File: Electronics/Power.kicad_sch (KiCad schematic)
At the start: 17 parts, among them U1 R-78C15-1.0, U401 R-78C5.0-1.0

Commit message: Updated Design
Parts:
- added H408, H409, H410, H411: MountingHole, MountingHole:MountingHole_3.2mm_M3_DIN965, symbol Mechanical:MountingHole
- C401, C403, C405: value C -> 4u7; footprint Capacitor_SMD:C_0603_1608Metric_Pad1.08x0.95mm_HandSolder -> Resistor_SMD:R_0805_2012Metric_Pad1.20x1.40mm_HandSolder
- C402, C404, C406, C407: value C -> 100n
- C408: value C -> 10u; footprint Capacitor_SMD:C_0603_1608Metric_Pad1.08x0.95mm_HandSolder -> Resistor_SMD:R_0805_2012Metric_Pad1.20x1.40mm_HandSolder
- renumbered U1 to U402
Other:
- moved on the sheet: C408
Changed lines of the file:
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@@
   (junction (at 199.39 53.34) (diameter 0) (color 0 0 0 0)
   )
-  (junction (at 250.19 53.34) (diameter 0) (color 0 0 0 0)
+  (junction (at 252.095 53.34) (diameter 0) (color 0 0 0 0)
   )
   (wire (pts (xy 209.55 53.34) (xy 209.55 55.88))
@@
     (stroke (width 0) (type default) (color 0 0 0 0))
   )
-  (wire (pts (xy 250.19 67.31) (xy 241.3 67.31))
+  (wire (pts (xy 252.095 67.31) (xy 241.3 67.31))
     (stroke (width 0) (type default) (color 0 0 0 0))
   )
@@
     (stroke (width 0) (type default) (color 0 0 0 0))
   )
-  (wire (pts (xy 250.19 53.34) (xy 259.08 53.34))
+  (wire (pts (xy 252.095 53.34) (xy 259.08 53.34))
     (stroke (width 0) (type default) (color 0 0 0 0))
   )
@@
     (stroke (width 0) (type default) (color 0 0 0 0))
   )
-  (wire (pts (xy 250.19 63.5) (xy 250.19 67.31))
-    (stroke (width 0) (type default) (color 0 0 0 0))
-  )
-  (wire (pts (xy 250.19 53.34) (xy 250.19 55.88))
+  (wire (pts (xy 252.095 63.5) (xy 252.095 67.31))
+    (stroke (width 0) (type default) (color 0 0 0 0))
+  )
+  (wire (pts (xy 252.095 53.34) (xy 252.095 55.88))
     (stroke (width 0) (type default) (color 0 0 0 0))
   )
@@
     (stroke (width 0) (type default) (color 0 0 0 0))
   )
-  (wire (pts (xy 241.3 53.34) (xy 250.19 53.34))
+  (wire (pts (xy 241.3 53.34) (xy 252.095 53.34))
     (stroke (width 0) (type default) (color 0 0 0 0))
   )
@@
     (pin "3")
   )
+  (symbol (lib_name "MountingHole_1") (lib_id "Mechanical:MountingHole") (at 135.89 191.77 0) (unit 1)
+    (in_bom yes) (on_board yes) (fields_autoplaced)
+    (property "Reference" "H409" (id 0) (at 138.43 190.8615 0)
+      (effects (font (size 1.27 1.27)) (justify left))
+    )
+    (property "Value" "MountingHole" (id 1) (at 138.43 193.6366 0)
+      (effects (font (size 1.27 1.27)) (justify left) hide)
+    )
+    (property "Footprint" "MountingHole:MountingHole_3.2mm_M3_DIN965" (id 2) (at 135.89 191.77 0)
+      (effects (font (size 1.27 1.27)) hide)
+    )
+    (property "Datasheet" "~" (id 3) (at 135.89 191.77 0)
+      (effects (font (size 1.27 1.27)) hide)
+    )
+  )
   (symbol (lib_name "MountingHole_1") (lib_id "Mechanical:MountingHole") (at 162.56 161.29 0) (unit 1)
     (in_bom yes) (on_board yes) (fields_autoplaced)
@@
       (effects (font (size 1.27 1.27)) (justify left))
     )
-    (property "Value" "C" (id 1) (at 202.311 61.5566 0)
-      (effects (font (size 1.27 1.27)) (justify left))
-    )
-    (property "Footprint" "Capacitor_SMD:C_0603_1608Metric_Pad1.08x0.95mm_HandSolder" (id 2) (at 200.3552 63.5 0)
+    (property "Value" "4u7" (id 1) (at 202.311 61.5566 0)
+      (effects (font (size 1.27 1.27)) (justify left))
+    )
+    (property "Footprint" "Resistor_SMD:R_0805_2012Metric_Pad1.20x1.40mm_HandSolder" (id 2) (at 200.3552 63.5 0)
       (effects (font (size 1.27 1.27)) hide)
     )
@@
       (effects (font (size 1.27 1.27)) (justify left))
     )
-    (property "Value" "C" (id 1) (at 96.901 61.5566 0)
-      (effects (font (size 1.27 1.27)) (justify left))
-    )
-    (property "Footprint" "Capacitor_SMD:C_0603_1608Metric_Pad1.08x0.95mm_HandSolder" (id 2) (at 94.9452 63.5 0)
+    (property "Value" "4u7" (id 1) (at 96.901 61.5566 0)
+      (effects (font (size 1.27 1.27)) (justify left))
+    )
+    (property "Footprint" "Resistor_SMD:R_0805_2012Metric_Pad1.20x1.40mm_HandSolder" (id 2) (at 94.9452 63.5 0)
       (effects (font (size 1.27 1.27)) hide)
     )
@@
   (symbol (lib_id "Regulator_Switching:R-78C15-1.0") (at 125.73 53.34 0) (unit 1)
     (in_bom yes) (on_board yes) (fields_autoplaced)
-    (property "Reference" "U1" (id 0) (at 125.73 45.72 0))
-    (property "Value" "R-78C15-1.0" (id 1) (at 125.73 48.26 0))
+    (property "Reference" "U402" (id 0) (at 125.73 47.4685 0))
+    (property "Value" "R-78C15-1.0" (id 1) (at 125.73 50.2436 0))
     (property "Footprint" "Converter_DCDC:Converter_DCDC_RECOM_R-78E-0.5_THT" (id 2) (at 127 59.69 0)
       (effects (font (size 1.27 1.27) italic) (justify left) hide)
@@
     (pin "3")
   )
+  (symbol (lib_name "MountingHole_1") (lib_id "Mechanical:MountingHole") (at 146.685 184.785 0) (unit 1)
+    (in_bom yes) (on_board yes) (fields_autoplaced)
+    (property "Reference" "H410" (id 0) (at 149.225 183.8765 0)
+      (effects (font (size 1.27 1.27)) (justify left))
+    )
+    (property "Value" "MountingHole" (id 1) (at 149.225 186.6516 0)
+      (effects (font (size 1.27 1.27)) (justify left) hide)
+    )
+    (property "Footprint" "MountingHole:MountingHole_3.2mm_M3_DIN965" (id 2) (at 146.685 184.785 0)
+      (effects (font (size 1.27 1.27)) hide)
+    )
+    (property "Datasheet" "~" (id 3) (at 146.685 184.785 0)
+      (effects (font (size 1.27 1.27)) hide)
+    )
+  )
   (symbol (lib_id "Device:C") (at 104.14 59.69 0) (unit 1)
     (in_bom yes) (on_board yes) (fields_autoplaced)
@@
       (effects (font (size 1.27 1.27)) (justify left))
     )
-    (property "Value" "C" (id 1) (at 107.061 61.5566 0)
+    (property "Value" "100n" (id 1) (at 107.061 61.5566 0)
       (effects (font (size 1.27 1.27)) (justify left))
     )
@@
       (effects (font (size 1.27 1.27)) (justify left))
     )
-    (property "Value" "C" (id 1) (at 244.221 61.5566 0)
+    (property "Value" "100n" (id 1) (at 244.221 61.5566 0)
       (effects (font (size 1.27 1.27)) (justify left))
     )
@@
       (effects (font (size 1.27 1.27)) (justify left))
     )
-    (property "Value" "C" (id 1) (at 212.471 61.5566 0)
+    (property "Value" "100n" (id 1) (at 212.471 61.5566 0)
       (effects (font (size 1.27 1.27)) (justify left))
     )
@@
       (effects (font (size 1.27 1.27)) (justify left))
     )
-    (property "Value" "C" (id 1) (at 147.701 61.5566 0)
-      (effects (font (size 1.27 1.27)) (justify left))
-    )
-    (property "Footprint" "Capacitor_SMD:C_0603_1608Metric_Pad1.08x0.95mm_HandSolder" (id 2) (at 145.7452 63.5 0)
+    (property "Value" "4u7" (id 1) (at 147.701 61.5566 0)
+      (effects (font (size 1.27 1.27)) (justify left))
+    )
+    (property "Footprint" "Resistor_SMD:R_0805_2012Metric_Pad1.20x1.40mm_HandSolder" (id 2) (at 145.7452 63.5 0)
       (effects (font (size 1.27 1.27)) hide)
     )
@@
     (pin "1")
   )
+  (symbol (lib_name "MountingHole_1") (lib_id "Mechanical:MountingHole") (at 135.89 184.785 0) (unit 1)
+    (in_bom yes) (on_board yes) (fields_autoplaced)
+    (property "Reference" "H408" (id 0) (at 138.43 183.8765 0)
+      (effects (font (size 1.27 1.27)) (justify left))
+    )
+    (property "Value" "MountingHole" (id 1) (at 138.43 186.6516 0)
+      (effects (font (size 1.27 1.27)) (justify left) hide)
+    )
+    (property "Footprint" "MountingHole:MountingHole_3.2mm_M3_DIN965" (id 2) (at 135.89 184.785 0)
+      (effects (font (size 1.27 1.27)) hide)
+    )
+    (property "Datasheet" "~" (id 3) (at 135.89 184.785 0)
+      (effects (font (size 1.27 1.27)) hide)
+    )
+  )
   (symbol (lib_id "Device:C") (at 154.94 59.69 0) (unit 1)
     (in_bom yes) (on_board yes) (fields_autoplaced)
@@
       (effects (font (size 1.27 1.27)) (justify left))
     )
-    (property "Value" "C" (id 1) (at 157.861 61.5566 0)
+    (property "Value" "100n" (id 1) (at 157.861 61.5566 0)
       (effects (font (size 1.27 1.27)) (justify left))
     )
@@
     (pin "1")
     (pin "2")
+  )
+  (symbol (lib_name "MountingHole_1") (lib_id "Mechanical:MountingHole") (at 146.685 191.77 0) (unit 1)
+    (in_bom yes) (on_board yes) (fields_autoplaced)
+    (property "Reference" "H411" (id 0) (at 149.225 190.8615 0)
+      (effects (font (size 1.27 1.27)) (justify left))
+    )
+    (property "Value" "MountingHole" (id 1) (at 149.225 193.6366 0)
+      (effects (font (size 1.27 1.27)) (justify left) hide)
+    )
+    (property "Footprint" "MountingHole:MountingHole_3.2mm_M3_DIN965" (id 2) (at 146.685 191.77 0)
+      (effects (font (size 1.27 1.27)) hide)
+    )
+    (property "Datasheet" "~" (id 3) (at 146.685 191.77 0)
+      (effects (font (size 1.27 1.27)) hide)
+    )
   )
   (symbol (lib_id "power:VD") (at 73.66 46.99 0) (unit 1)
@@
     (pin "1")
   )
-  (symbol (lib_id "Device:C") (at 250.19 59.69 0) (unit 1)
-    (in_bom yes) (on_board yes) (fields_autoplaced)
-    (property "Reference" "C408" (id 0) (at 253.111 58.7815 0)
-      (effects (font (size 1.27 1.27)) (justify left))
-    )
-    (property "Value" "C" (id 1) (at 253.111 61.5566 0)
-      (effects (font (size 1.27 1.27)) (justify left))
-    )
-    (property "Footprint" "Capacitor_SMD:C_0603_1608Metric_Pad1.08x0.95mm_HandSolder" (id 2) (at 251.1552 63.5 0)
-      (effects (font (size 1.27 1.27)) hide)
-    )
-    (property "Datasheet" "~" (id 3) (at 250.19 59.69 0)
-      (effects (font (size 1.27 1.27)) hide)
-    )
+  (symbol (lib_id "Device:C") (at 252.095 59.69 0) (unit 1)
+    (in_bom yes) (on_board yes) (fields_autoplaced)
+    (property "Reference" "C408" (id 0) (at 255.016 58.7815 0)
+      (effects (font (size 1.27 1.27)) (justify left))
+    )
+    (property "Value" "10u" (id 1) (at 255.016 61.5566 0)
+      (effects (font (size 1.27 1.27)) (justify left))
+    )
+    (property "Footprint" "Resistor_SMD:R_0805_2012Metric_Pad1.20x1.40mm_HandSolder" (id 2) (at 253.0602 63.5 0)
+      (effects (font (size 1.27 1.27)) hide)
+    )
+    (property "Datasheet" "~" (id 3) (at 252.095 59.69 0)
+      (effects (font (size 1.27 1.27)) hide)
+    )

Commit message: Layout improvements
Signed-off-by: Aki Kuusela <git@findersee.fi>
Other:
- company: (none) -> findersee.fi
- title: (none) -> Motor Controller
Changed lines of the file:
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@@
 (kicad_sch (version 20211123) (generator eeschema)
   (paper "A4")
+  (title_block
+    (title "Motor Controller")
+    (date "2022-02-18")
+    (rev "1.0")
+    (company "findersee.fi")
+  )
   (junction (at 166.37 53.34) (diameter 0) (color 0 0 0 0)
   )

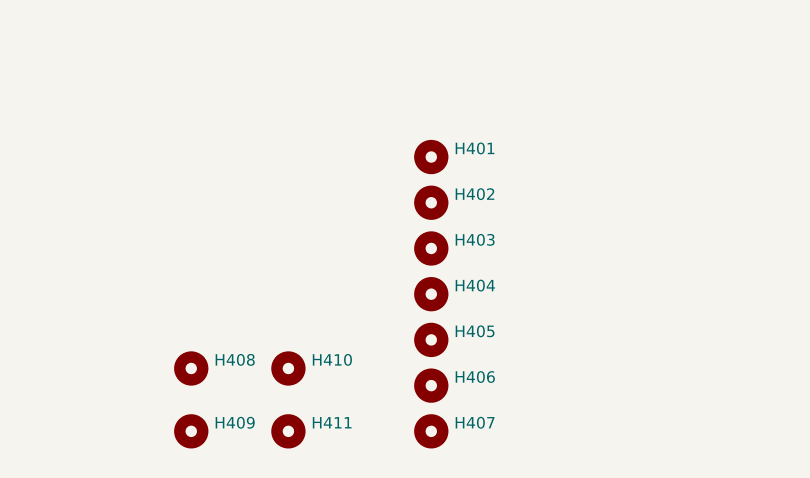
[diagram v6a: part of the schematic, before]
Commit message: Changed capacitor to multi footprint version. Added parallel diodes to MOSFET gate resistors to improve Turn-OFF time.
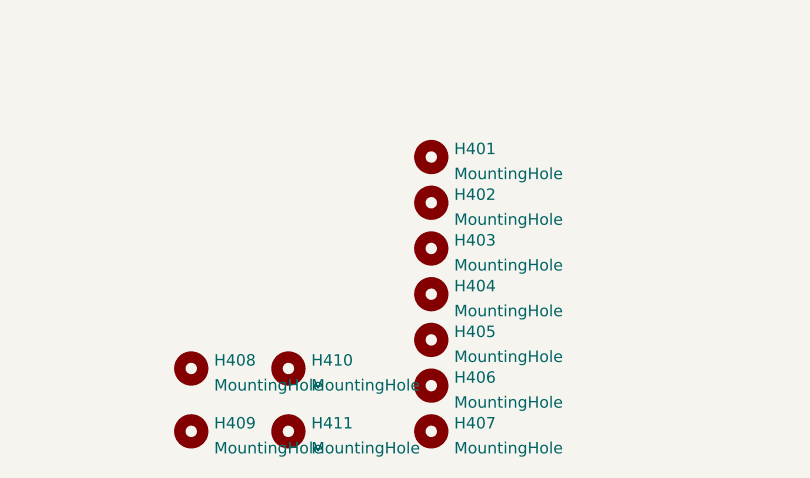
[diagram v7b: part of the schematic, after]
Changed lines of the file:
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@@
     )
     (property "Value" "MountingHole" (id 1) (at 138.43 193.6366 0)
-      (effects (font (size 1.27 1.27)) (justify left) hide)
+      (effects (font (size 1.27 1.27)) (justify left))
     )
     (property "Footprint" "MountingHole:MountingHole_3.2mm_M3_DIN965" (id 2) (at 135.89 191.77 0)
@@
     )
     (property "Value" "MountingHole" (id 1) (at 165.1 163.1566 0)
-      (effects (font (size 1.27 1.27)) (justify left) hide)
+      (effects (font (size 1.27 1.27)) (justify left))
     )
     (property "Footprint" "MountingHole:MountingHole_3.2mm_M3_DIN965" (id 2) (at 162.56 161.29 0)
@@
     )
     (property "Value" "MountingHole" (id 1) (at 165.1 178.3966 0)
-      (effects (font (size 1.27 1.27)) (justify left) hide)
+      (effects (font (size 1.27 1.27)) (justify left))
     )
     (property "Footprint" "MountingHole:MountingHole_3.2mm_M3_DIN965" (id 2) (at 162.56 176.53 0)
@@
     )
     (property "Value" "MountingHole" (id 1) (at 149.225 186.6516 0)
-      (effects (font (size 1.27 1.27)) (justify left) hide)
+      (effects (font (size 1.27 1.27)) (justify left))
     )
     (property "Footprint" "MountingHole:MountingHole_3.2mm_M3_DIN965" (id 2) (at 146.685 184.785 0)
@@
     )
     (property "Value" "MountingHole" (id 1) (at 165.1 168.2366 0)
-      (effects (font (size 1.27 1.27)) (justify left) hide)
+      (effects (font (size 1.27 1.27)) (justify left))
     )
     (property "Footprint" "MountingHole:MountingHole_3.2mm_M3_DIN965" (id 2) (at 162.56 166.37 0)
@@
     )
     (property "Value" "MountingHole" (id 1) (at 165.1 173.3166 0)
-      (effects (font (size 1.27 1.27)) (justify left) hide)
+      (effects (font (size 1.27 1.27)) (justify left))
     )
     (property "Footprint" "MountingHole:MountingHole_3.2mm_M3_DIN965" (id 2) (at 162.56 171.45 0)
@@
     )
     (property "Value" "MountingHole" (id 1) (at 165.1 188.5566 0)
-      (effects (font (size 1.27 1.27)) (justify left) hide)
+      (effects (font (size 1.27 1.27)) (justify left))
     )
     (property "Footprint" "MountingHole:MountingHole_3.2mm_M3_DIN965" (id 2) (at 162.56 186.69 0)
@@
     )
     (property "Value" "MountingHole" (id 1) (at 138.43 186.6516 0)
-      (effects (font (size 1.27 1.27)) (justify left) hide)
+      (effects (font (size 1.27 1.27)) (justify left))
     )
     (property "Footprint" "MountingHole:MountingHole_3.2mm_M3_DIN965" (id 2) (at 135.89 184.785 0)
@@
     )
     (property "Value" "MountingHole" (id 1) (at 149.225 193.6366 0)
-      (effects (font (size 1.27 1.27)) (justify left) hide)
+      (effects (font (size 1.27 1.27)) (justify left))
     )
     (property "Footprint" "MountingHole:MountingHole_3.2mm_M3_DIN965" (id 2) (at 146.685 191.77 0)
@@
     )
     (property "Value" "MountingHole" (id 1) (at 165.1 183.4766 0)
-      (effects (font (size 1.27 1.27)) (justify left) hide)
+      (effects (font (size 1.27 1.27)) (justify left))
     )
     (property "Footprint" "MountingHole:MountingHole_3.2mm_M3_DIN965" (id 2) (at 162.56 181.61 0)
@@
     )
     (property "Value" "MountingHole" (id 1) (at 165.1 193.6366 0)
-      (effects (font (size 1.27 1.27)) (justify left) hide)
+      (effects (font (size 1.27 1.27)) (justify left))
     )
     (property "Footprint" "MountingHole:MountingHole_3.2mm_M3_DIN965" (id 2) (at 162.56 191.77 0)

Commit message: Manufacturing commit of PCB
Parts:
- added C409: 4u7, Resistor_SMD:R_0805_2012Metric_Pad1.20x1.40mm_HandSolder, symbol Device:C
- added C410, C411: 100n, Capacitor_SMD:C_0603_1608Metric_Pad1.08x0.95mm_HandSolder, symbol Device:C
- added C412: 10u, Resistor_SMD:R_0805_2012Metric_Pad1.20x1.40mm_HandSolder, symbol Device:C
- added U400: R-78C3.3-1.0, Converter_DCDC:Converter_DCDC_RECOM_R-78E-0.5_THT, symbol Regulator_Switching:R-78C3.3-1.0
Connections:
- net GND: now also C409.2, C410.2, C411.2, C412.2, U400.2 (GND)
- net VCC: now also C409.1, C410.1, U400.1 (IN)
- new net +3V3: C411.1, C412.1, U400.3 (OUT)
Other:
- note added: "Heatsink Mounting holes M3"
- note added: "PCB Mounting holes M3"
- moved on the sheet: H408, H409, H410, H411
